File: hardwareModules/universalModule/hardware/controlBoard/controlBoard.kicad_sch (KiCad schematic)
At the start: 20 parts, among them J10 INTERFACE_CONN_TOP, J11 CONTROL_BOARD_CONN, J7 BATTERY_BOARD_CONN, J9 INTERFACE_CONN_BOTTOM, U1 Servo, U2 Servo

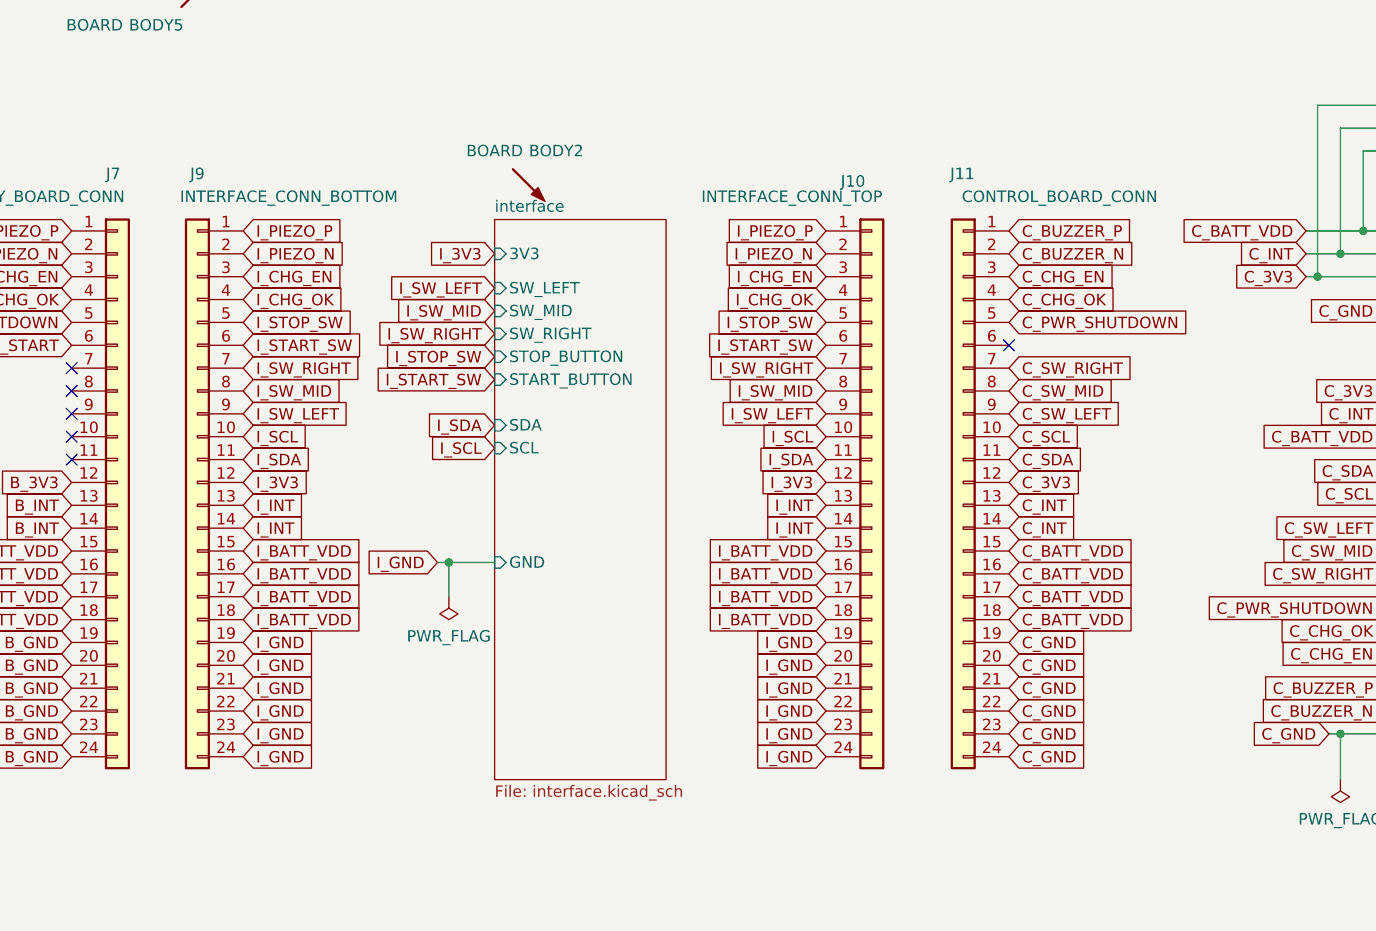
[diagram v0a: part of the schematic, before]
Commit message: um: Fix hardware bugs, prepare v0.5
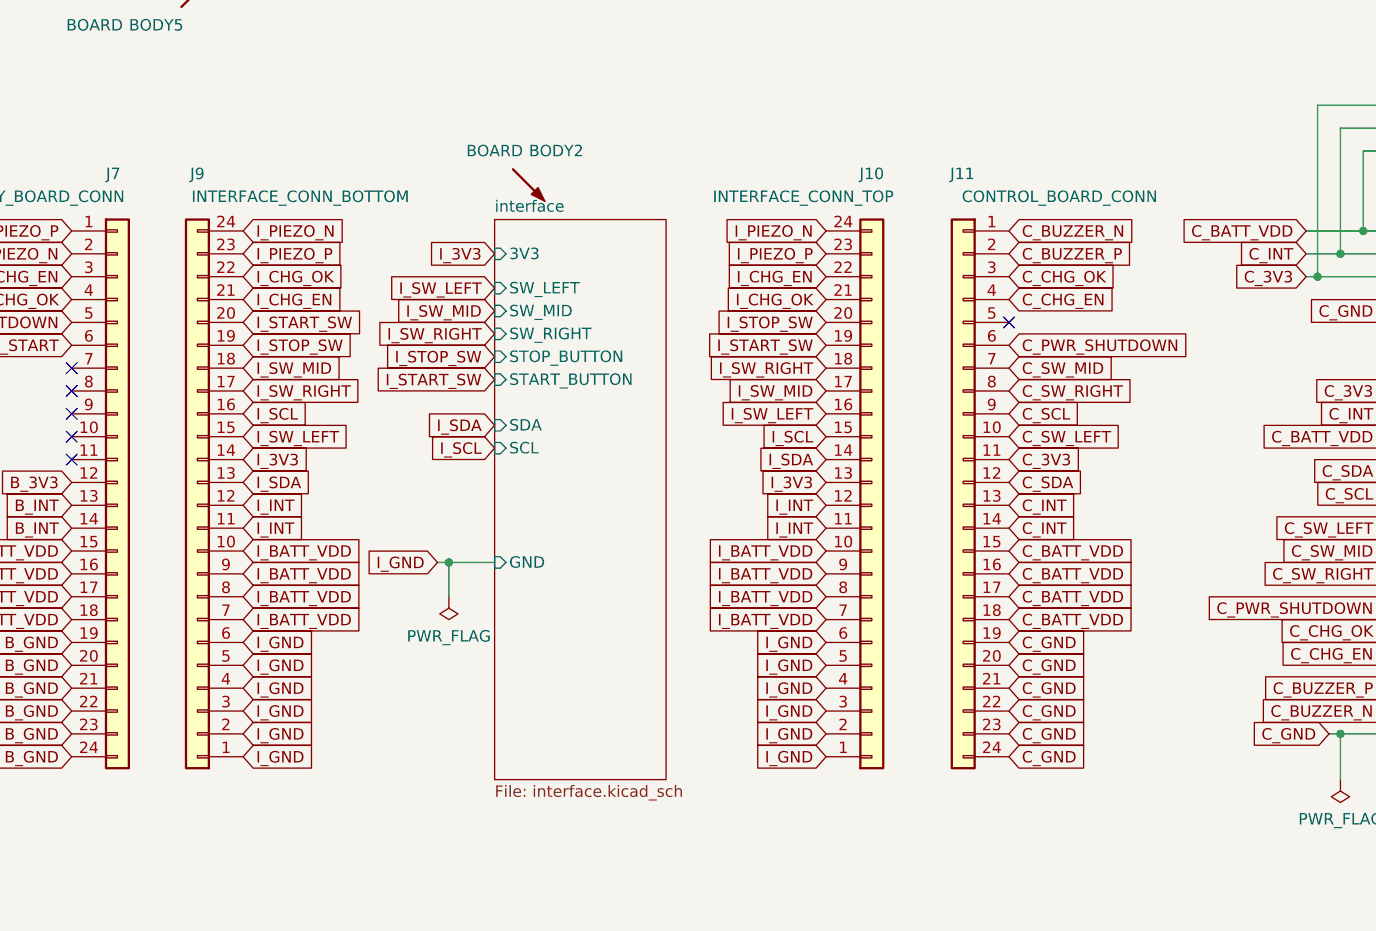
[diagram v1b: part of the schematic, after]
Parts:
- J11: MFR A3C-24P-2DSA(30) -> TMM-112-06-T-D-SM
- J9: footprint rofi:2xM22-6550642R-MIRRORED -> Connector_PinHeader_2.00mm:PinHeader_2x12_P2.00mm_Vertical
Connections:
- net C_3V3: now also J11.11 (Pin_11); no longer J11.12 (Pin_12)
- net C_BUZZER_N: now also J11.1 (Pin_1); no longer J11.2 (Pin_2)
- net C_BUZZER_P: now also J11.2 (Pin_2); no longer J11.1 (Pin_1)
- net C_CHG_EN: now also J11.4 (Pin_4); no longer J11.3 (Pin_3)
- net C_CHG_OK: now also J11.3 (Pin_3); no longer J11.4 (Pin_4)
- net C_PWR_SHUTDOWN: now also J11.6 (Pin_6); no longer J11.5 (Pin_5)
- net C_SCL: now also J11.9 (Pin_9); no longer J11.10 (Pin_10)
- net C_SDA: now also J11.12 (Pin_12); no longer J11.11 (Pin_11)
- net C_SW_LEFT: now also J11.10 (Pin_10); no longer J11.9 (Pin_9)
- net C_SW_MID: now also J11.7 (Pin_7); no longer J11.8 (Pin_8)
- net C_SW_RIGHT: now also J11.8 (Pin_8); no longer J11.7 (Pin_7)
- net I_3V3: now also J10.13 (Pin_13), J9.14 (Pin_14); no longer J10.12 (Pin_12), J9.12 (Pin_12)
- net I_BATT_VDD: now also J10.10 (Pin_10), J10.7 (Pin_7), J10.8 (Pin_8), J10.9 (Pin_9), J9.10 (Pin_10), J9.7 (Pin_7), J9.8 (Pin_8), J9.9 (Pin_9); no longer J10.15 (Pin_15), J10.16 (Pin_16), J10.17 (Pin_17), J10.18 (Pin_18), J9.15 (Pin_15), J9.16 (Pin_16), J9.17 (Pin_17), J9.18 (Pin_18)
- net I_CHG_EN: now also J10.22 (Pin_22), J9.21 (Pin_21); no longer J10.3 (Pin_3), J9.3 (Pin_3)
- net I_CHG_OK: now also J10.21 (Pin_21), J9.22 (Pin_22); no longer J10.4 (Pin_4), J9.4 (Pin_4)
- net I_GND: now also J10.1 (Pin_1), J10.2 (Pin_2), J10.3 (Pin_3), J10.4 (Pin_4), J10.5 (Pin_5), J10.6 (Pin_6), J9.1 (Pin_1), J9.2 (Pin_2), J9.3 (Pin_3), J9.4 (Pin_4), J9.5 (Pin_5), J9.6 (Pin_6); no longer J10.19 (Pin_19), J10.20 (Pin_20), J10.21 (Pin_21), J10.22 (Pin_22), J10.23 (Pin_23), J10.24 (Pin_24), J9.19 (Pin_19), J9.20 (Pin_20), J9.21 (Pin_21), J9.22 (Pin_22), J9.23 (Pin_23), J9.24 (Pin_24)
- net I_INT: now also J10.11 (Pin_11), J10.12 (Pin_12), J9.11 (Pin_11), J9.12 (Pin_12); no longer J10.13 (Pin_13), J10.14 (Pin_14), J9.13 (Pin_13), J9.14 (Pin_14)
- net I_PIEZO_N: now also J10.24 (Pin_24), J9.24 (Pin_24); no longer J10.2 (Pin_2), J9.2 (Pin_2)
- net I_PIEZO_P: now also J10.23 (Pin_23), J9.23 (Pin_23); no longer J10.1 (Pin_1), J9.1 (Pin_1)
- net I_SCL: now also J10.15 (Pin_15), J9.16 (Pin_16); no longer J10.10 (Pin_10), J9.10 (Pin_10)
- net I_SDA: now also J10.14 (Pin_14), J9.13 (Pin_13); no longer J10.11 (Pin_11), J9.11 (Pin_11)
- net I_START_SW: now also J10.19 (Pin_19), J9.20 (Pin_20); no longer J10.6 (Pin_6), J9.6 (Pin_6)
- net I_STOP_SW: now also J10.20 (Pin_20), J9.19 (Pin_19); no longer J10.5 (Pin_5), J9.5 (Pin_5)
- net I_SW_LEFT: now also J10.16 (Pin_16), J9.15 (Pin_15); no longer J10.9 (Pin_9), J9.9 (Pin_9)
- net I_SW_MID: now also J10.17 (Pin_17), J9.18 (Pin_18); no longer J10.8 (Pin_8), J9.8 (Pin_8)
- net I_SW_RIGHT: now also J10.18 (Pin_18), J9.17 (Pin_17); no longer J10.7 (Pin_7), J9.7 (Pin_7)
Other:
- moved on the sheet: J9
